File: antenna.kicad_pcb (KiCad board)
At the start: 2 copper layers, 158.4 x 158.4 mm, 10 parts, among them J1 Conn_Coaxial, J2 Conn_Coaxial

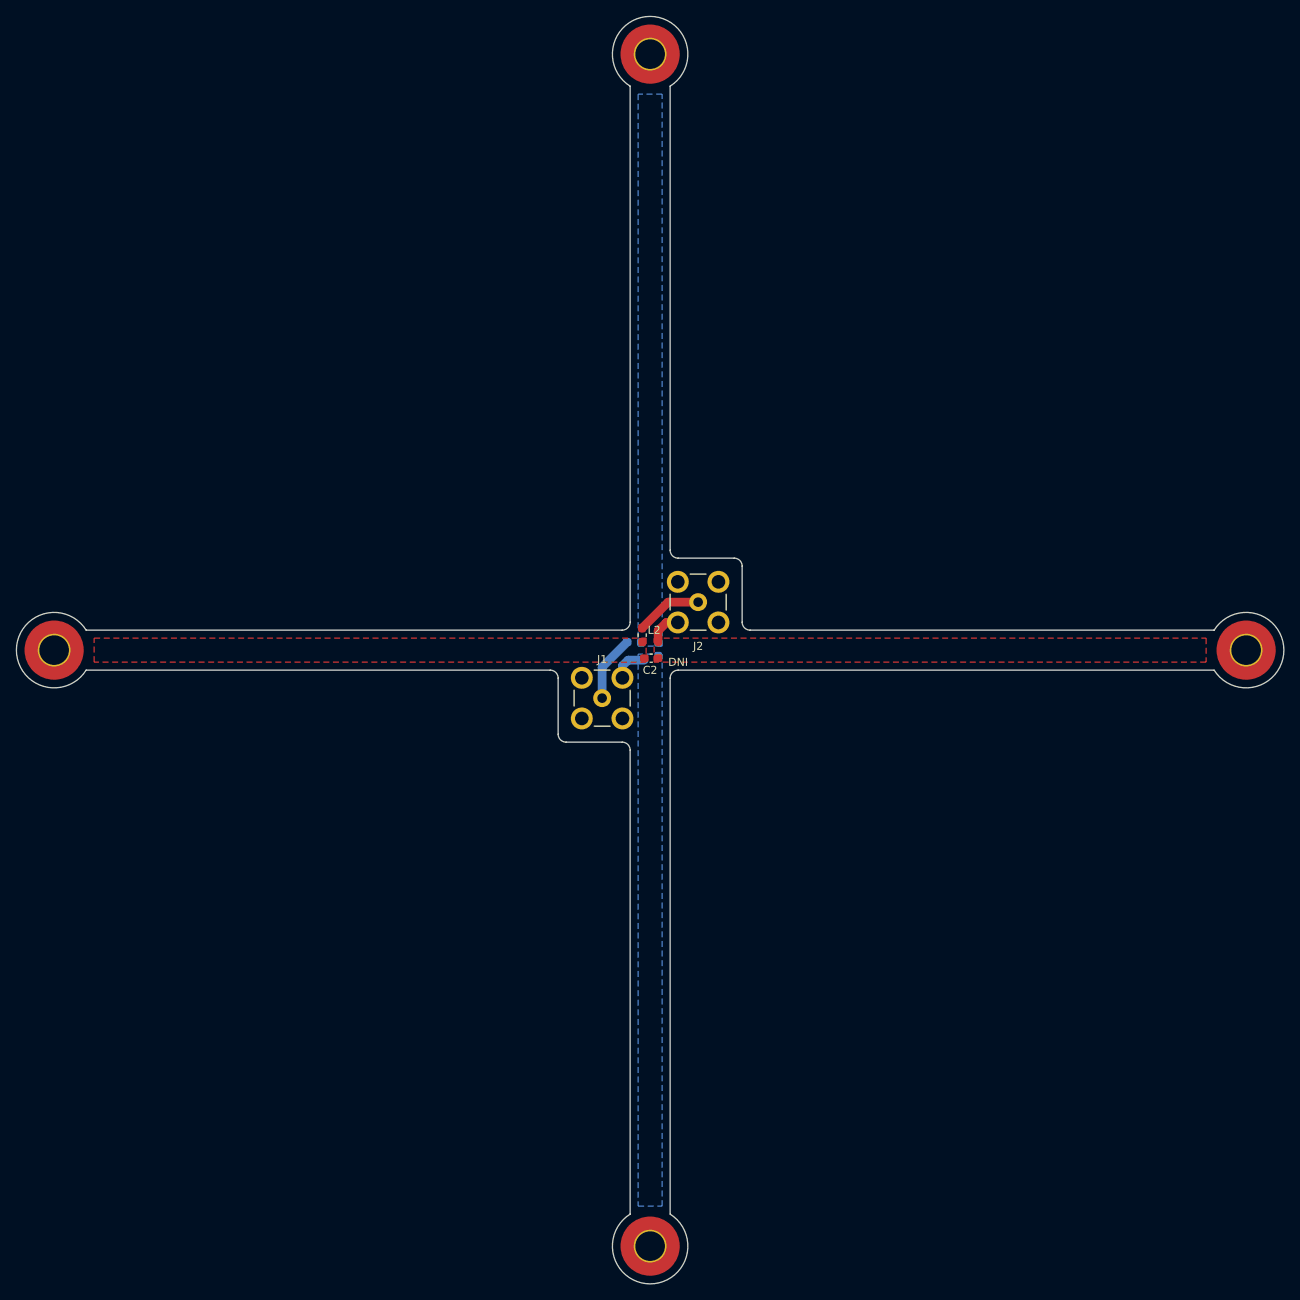
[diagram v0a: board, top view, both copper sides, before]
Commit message: Edit silkscreen and generate gerbers
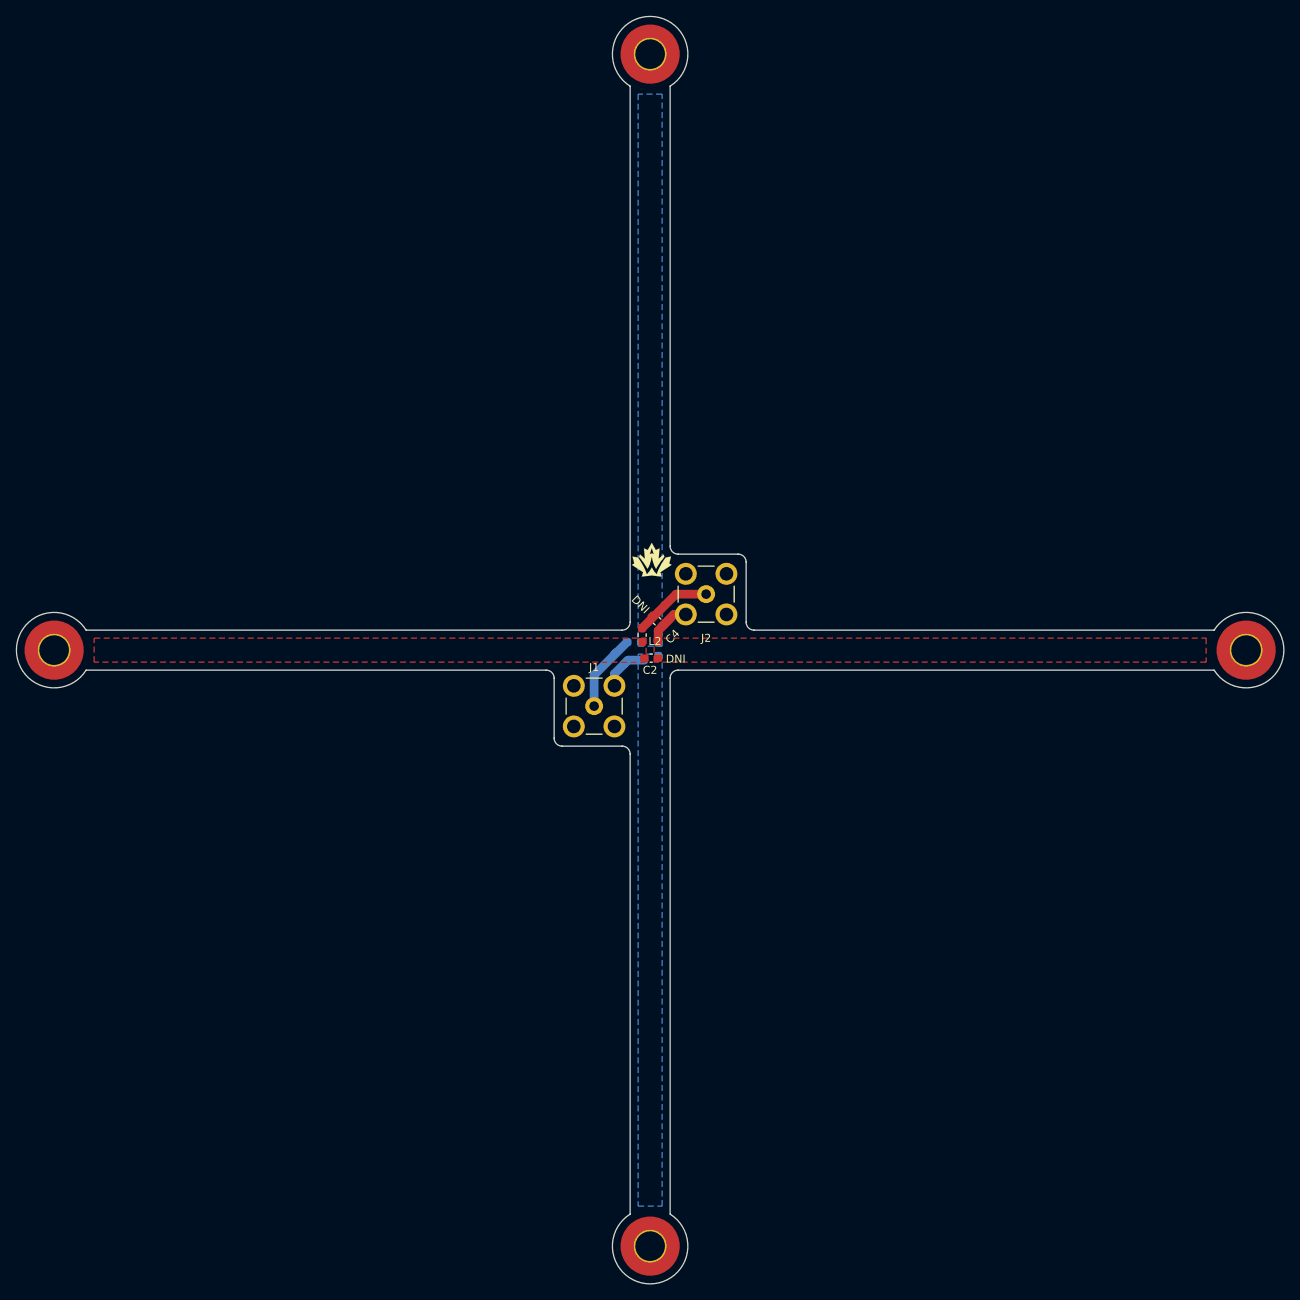
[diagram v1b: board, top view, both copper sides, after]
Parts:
- added C3: DNI, Capacitor_SMD:C_0603_1608Metric_Pad1.08x0.95mm_HandSolder, B.Cu at (131.2, 109.5)
- added C4: DNI, Capacitor_SMD:C_0603_1608Metric_Pad1.08x0.95mm_HandSolder, F.Cu at (135.9, 104.9)
- added G***: LOGO, Team_Logo:Logo_SilkScreen_5mm, F.Cu at (135.2, 97.2)
- moved J1 1.41 mm to (128.0, 115.5)
- moved J2 1.41 mm to (142.0, 101.5)
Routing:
- net /ANT2_N: track 4.31 -> 7.16 mm
- net Net-(J1-Pad1): track 8.29 -> 9.71 mm
- net /ANT1_N: track 4.50 -> 5.92 mm
- net Net-(J2-Pad1): track 8.35 -> 9.76 mm
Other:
- outline, holes or cut-outs redrawn

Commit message: remove mounting points
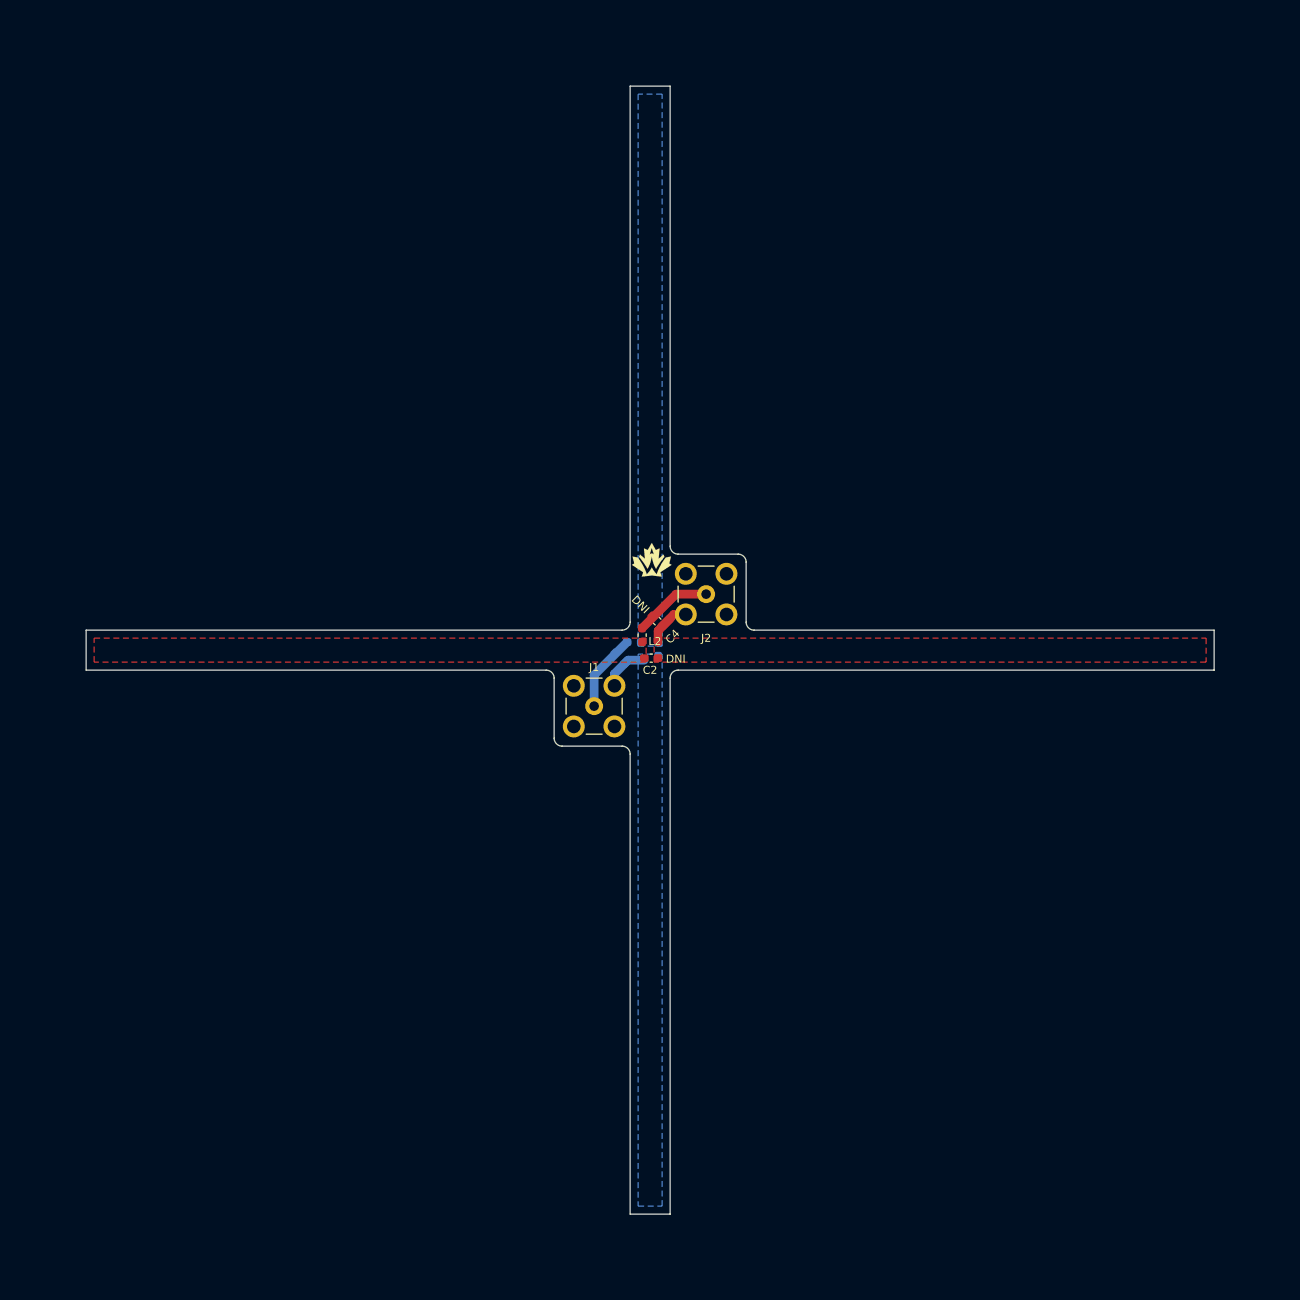
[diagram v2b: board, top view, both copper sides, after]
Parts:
- removed REF** (x4): MountingHole_3.7mm_Pad_TopOnly, MountingHole:MountingHole_3.7mm_Pad_TopOnly
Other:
- board size 158.4 x 158.4 mm -> 141 x 141 mm
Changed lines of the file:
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@@
     )
-  )
-  (footprint "MountingHole:MountingHole_3.7mm_Pad_TopOnly" (layer "F.Cu")
-    (at 135 183)
-    (descr "Mounting Hole 3.7mm")
-    (tags "mounting hole 3.7mm")
-    (attr exclude_from_pos_files exclude_from_bom)
-    (fp_text reference "REF**" (at 0 -4.7) (layer "F.SilkS") hide
-      (effects (font (size 1 1) (thickness 0.15)))
-    )
-    (fp_text value "MountingHole_3.7mm_Pad_TopOnly" (at 0 4.7) (layer "F.Fab") hide
-      (effects (font (size 1 1) (thickness 0.15)))
-    )
-    (fp_text user "${REFERENCE}" (at 0 0) (layer "F.Fab") hide
-      (effects (font (size 1 1) (thickness 0.15)))
-    )
-    (fp_circle (center 0 0) (end 3.7 0) (layer "Cmts.User") (width 0.15) (fill none))
-    (fp_circle (center 0 0) (end 3.95 0) (layer "F.CrtYd") (width 0.05) (fill none))
-    (pad "1" connect circle (at 0 0) (size 7.4 7.4) (layers "F.Cu" "F.Mask"))
-    (pad "1" thru_hole circle (at 0 0) (size 4.1 4.1) (drill 3.7) (layers *.Cu *.Mask))
   )
   (footprint "Team_Logo:Logo_SilkScreen_5mm" (layer "F.Cu")
@@
       ) (layer "F.SilkS") (width 0.01) (fill solid))
   )
-  (footprint "MountingHole:MountingHole_3.7mm_Pad_TopOnly" (layer "F.Cu")
-    (at 60.5 108.5)
-    (descr "Mounting Hole 3.7mm")
-    (tags "mounting hole 3.7mm")
-    (attr exclude_from_pos_files exclude_from_bom)
-    (fp_text reference "REF**" (at 0 -4.7) (layer "F.SilkS") hide
-      (effects (font (size 1 1) (thickness 0.15)))
-    )
-    (fp_text value "MountingHole_3.7mm_Pad_TopOnly" (at 0 4.7) (layer "F.Fab") hide
-      (effects (font (size 1 1) (thickness 0.15)))
-    )
-    (fp_text user "${REFERENCE}" (at 0 0) (layer "F.Fab") hide
-      (effects (font (size 1 1) (thickness 0.15)))
-    )
-    (fp_circle (center 0 0) (end 3.7 0) (layer "Cmts.User") (width 0.15) (fill none))
-    (fp_circle (center 0 0) (end 3.95 0) (layer "F.CrtYd") (width 0.05) (fill none))
-    (pad "1" thru_hole circle (at 0 0) (size 4.1 4.1) (drill 3.7) (layers *.Cu *.Mask))
-    (pad "1" connect circle (at 0 0) (size 7.4 7.4) (layers "F.Cu" "F.Mask"))
-  )
-  (footprint "MountingHole:MountingHole_3.7mm_Pad_TopOnly" (layer "F.Cu")
-    (at 135 34)
-    (descr "Mounting Hole 3.7mm")
-    (tags "mounting hole 3.7mm")
-    (attr exclude_from_pos_files exclude_from_bom)
-    (fp_text reference "REF**" (at 0 -4.7) (layer "F.SilkS") hide
-      (effects (font (size 1 1) (thickness 0.15)))
-    )
-    (fp_text value "MountingHole_3.7mm_Pad_TopOnly" (at 0 4.7) (layer "F.Fab") hide
-      (effects (font (size 1 1) (thickness 0.15)))
-    )
-    (fp_text user "${REFERENCE}" (at 0 0) (layer "F.Fab") hide
-      (effects (font (size 1 1) (thickness 0.15)))
-    )
-    (fp_circle (center 0 0) (end 3.7 0) (layer "Cmts.User") (width 0.15) (fill none))
-    (fp_circle (center 0 0) (end 3.95 0) (layer "F.CrtYd") (width 0.05) (fill none))
-    (pad "1" connect circle (at 0 0) (size 7.4 7.4) (layers "F.Cu" "F.Mask"))
-    (pad "1" thru_hole circle (at 0 0) (size 4.1 4.1) (drill 3.7) (layers *.Cu *.Mask))
-  )
-  (footprint "MountingHole:MountingHole_3.7mm_Pad_TopOnly" (layer "F.Cu")
-    (at 209.5 108.5)
-    (descr "Mounting Hole 3.7mm")
-    (tags "mounting hole 3.7mm")
-    (attr exclude_from_pos_files exclude_from_bom)
-    (fp_text reference "REF**" (at 0 -4.7) (layer "F.SilkS") hide
-      (effects (font (size 1 1) (thickness 0.15)))
-    )
-    (fp_text value "MountingHole_3.7mm_Pad_TopOnly" (at 0 4.7) (layer "F.Fab") hide
-      (effects (font (size 1 1) (thickness 0.15)))
-    )
-    (fp_text user "${REFERENCE}" (at 0 0) (layer "F.Fab") hide
-      (effects (font (size 1 1) (thickness 0.15)))
-    )
-    (fp_circle (center 0 0) (end 3.7 0) (layer "Cmts.User") (width 0.15) (fill none))
-    (fp_circle (center 0 0) (end 3.95 0) (layer "F.CrtYd") (width 0.05) (fill none))
-    (pad "1" thru_hole circle (at 0 0) (size 4.1 4.1) (drill 3.7) (layers *.Cu *.Mask))
-    (pad "1" connect circle (at 0 0) (size 7.4 7.4) (layers "F.Cu" "F.Mask"))
-  )
   (footprint "Inductor_SMD:L_0603_1608Metric_Pad1.05x0.95mm_HandSolder" (layer "B.Cu")
     (at 133 107.5 180)
@@
   (gr_line (start 147 97.5) (end 147 105) (layer "Edge.Cuts") (width 0.1))
   (gr_arc (start 148 106) (mid 147.292893 105.707107) (end 147 105) (layer "Edge.Cuts") (width 0.1))
-  (gr_arc (start 137.5 179) (mid 135 187.716991) (end 132.5 179) (layer "Edge.Cuts") (width 0.1))
-  (gr_arc (start 132.5 38) (mid 135 29.283009) (end 137.5 38) (layer "Edge.Cuts") (width 0.1))
   (gr_line (start 132.5 105) (end 132.5 38) (layer "Edge.Cuts") (width 0.1))
-  (gr_arc (start 205.5 106) (mid 214.216991 108.5) (end 205.5 111) (layer "Edge.Cuts") (width 0.1))
-  (gr_arc (start 64.5 111) (mid 55.783009 108.5) (end 64.499999 106) (layer "Edge.Cuts") (width 0.1))
   (gr_arc (start 131.5 120.5) (mid 132.207107 120.792893) (end 132.5 121.5) (layer "Edge.Cuts") (width 0.1))
   (gr_line (start 122 111) (end 64.5 111) (layer "Edge.Cuts") (width 0.1))
   (gr_arc (start 137.5 112) (mid 137.792893 111.292893) (end 138.5 111) (layer "Edge.Cuts") (width 0.1))
+  (gr_line (start 137.5 179) (end 132.5 179) (layer "Edge.Cuts") (width 0.1))
   (gr_arc (start 132.5 105) (mid 132.207107 105.707107) (end 131.5 106) (layer "Edge.Cuts") (width 0.1))
   (gr_line (start 137.5 38) (end 137.5 95.5) (layer "Edge.Cuts") (width 0.1))
+  (gr_line (start 205.5 111) (end 205.5 106) (layer "Edge.Cuts") (width 0.1))
   (gr_line (start 205.5 111) (end 138.5 111) (layer "Edge.Cuts") (width 0.1))
   (gr_line (start 138.5 96.5) (end 146 96.5) (layer "Edge.Cuts") (width 0.1))
@@
   (gr_arc (start 124 120.5) (mid 123.292893 120.207107) (end 123 119.5) (layer "Edge.Cuts") (width 0.1))
   (gr_line (start 131.5 120.5) (end 124 120.5) (layer "Edge.Cuts") (width 0.1))
+  (gr_line (start 137.5 38) (end 132.5 38) (layer "Edge.Cuts") (width 0.1))
+  (gr_line (start 64.5 111) (end 64.499999 106) (layer "Edge.Cuts") (width 0.1))
   (gr_line (start 148 106) (end 205.5 106) (layer "Edge.Cuts") (width 0.1))
   (gr_line (start 132.5 179) (end 132.5 121.5) (layer "Edge.Cuts") (width 0.1))

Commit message: Made Single Antenna
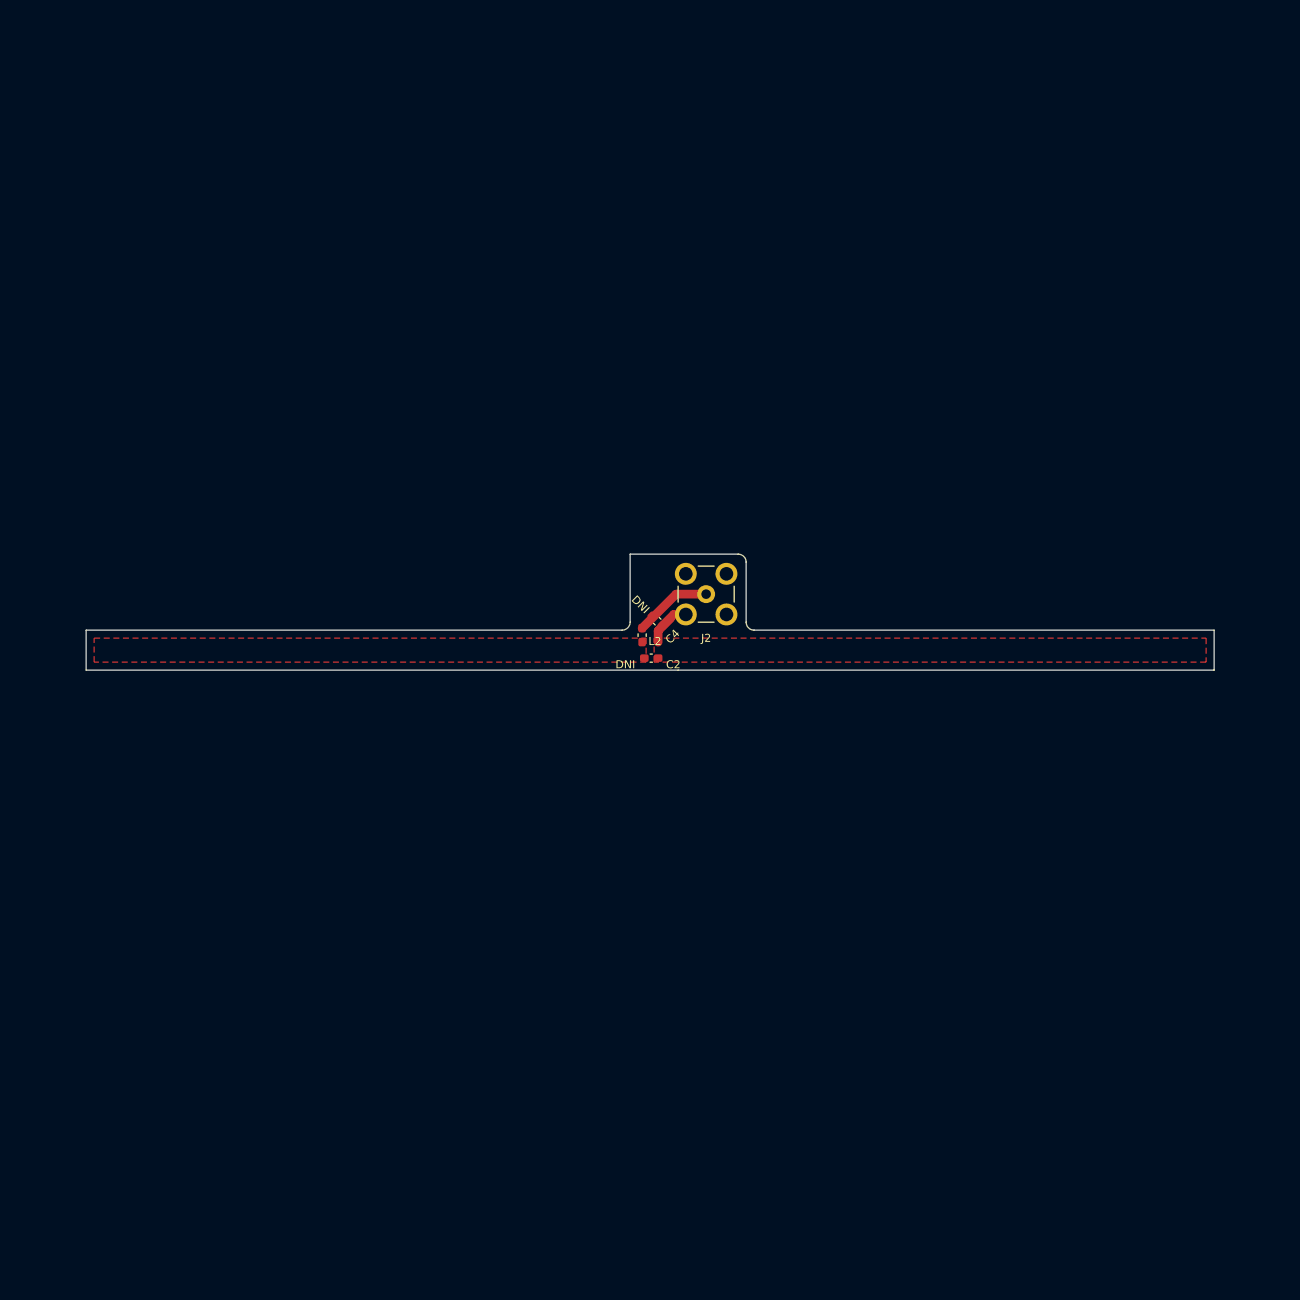
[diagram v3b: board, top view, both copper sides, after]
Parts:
- removed C1, C3: DNI, Capacitor_SMD:C_0603_1608Metric_Pad1.08x0.95mm_HandSolder
- removed G***: LOGO, Team_Logo:Logo_SilkScreen_5mm
- removed J1: Conn_Coaxial, Connector_Coaxial:SMB_Jack_Vertical
- removed L1: 12n5, Inductor_SMD:L_0603_1608Metric_Pad1.05x0.95mm_HandSolder
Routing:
- net Net-(J1-Pad1): track 9.71 -> 0.00 mm
- net /ANT1_N: track 5.92 -> 0.00 mm
- removed copper zone on B.Cu, net /ANT1_N
- removed copper zone on B.Cu, net /ANT1_P
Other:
- board size 141 x 141 mm -> 141 x 14.5 mm
